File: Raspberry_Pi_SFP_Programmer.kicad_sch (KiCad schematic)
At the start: 18 parts, among them J1 RPi_GPIO, J2 SFP+, J4 Conn_02x03_Odd_Even, Q1 BC847, Q2 BC847

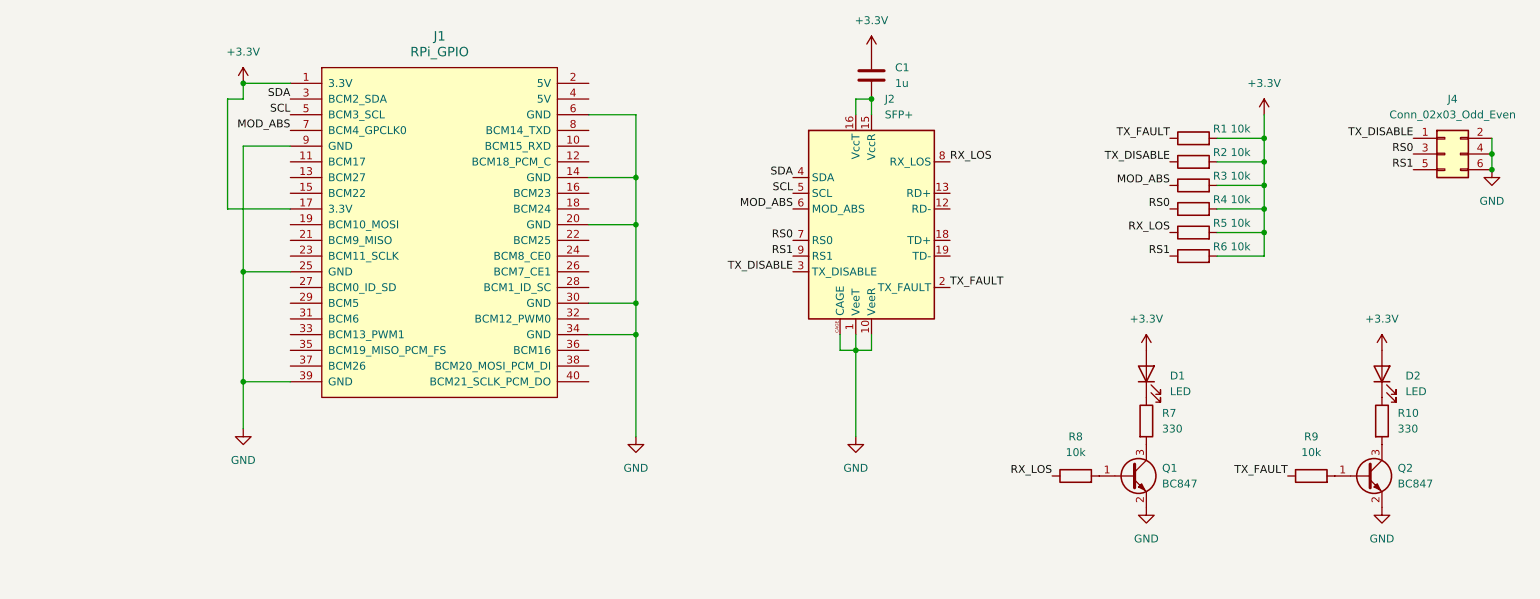
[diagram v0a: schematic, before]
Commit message: Fix PSU cap
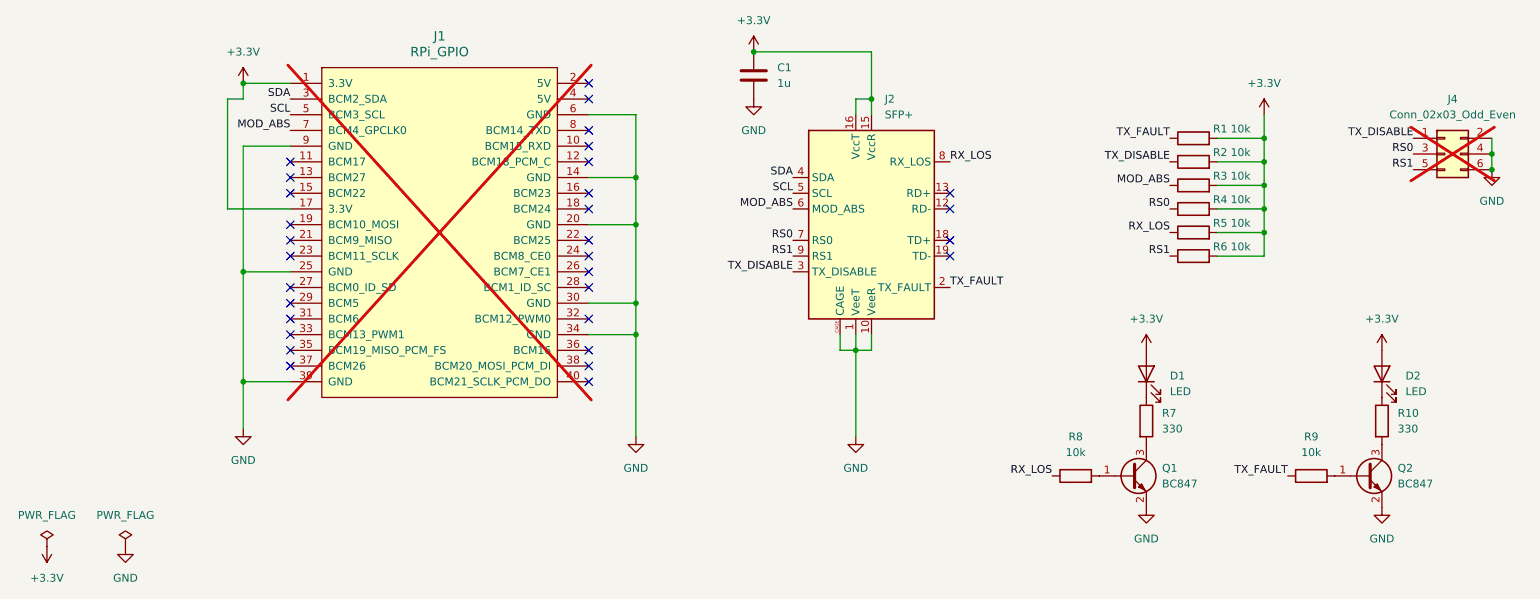
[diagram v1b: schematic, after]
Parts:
- J1, J4: now not fitted
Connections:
- net +3.3V: now also J2.15 (VccR), J2.16 (VccT)
- net GND: now also C1.2
- no-connect marks 0 -> 31
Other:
- moved on the sheet: C1
